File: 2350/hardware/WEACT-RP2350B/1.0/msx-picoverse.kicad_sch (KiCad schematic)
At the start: 10 parts, among them J1 Micro_SD_Card, U1 WEACT-RP2350B

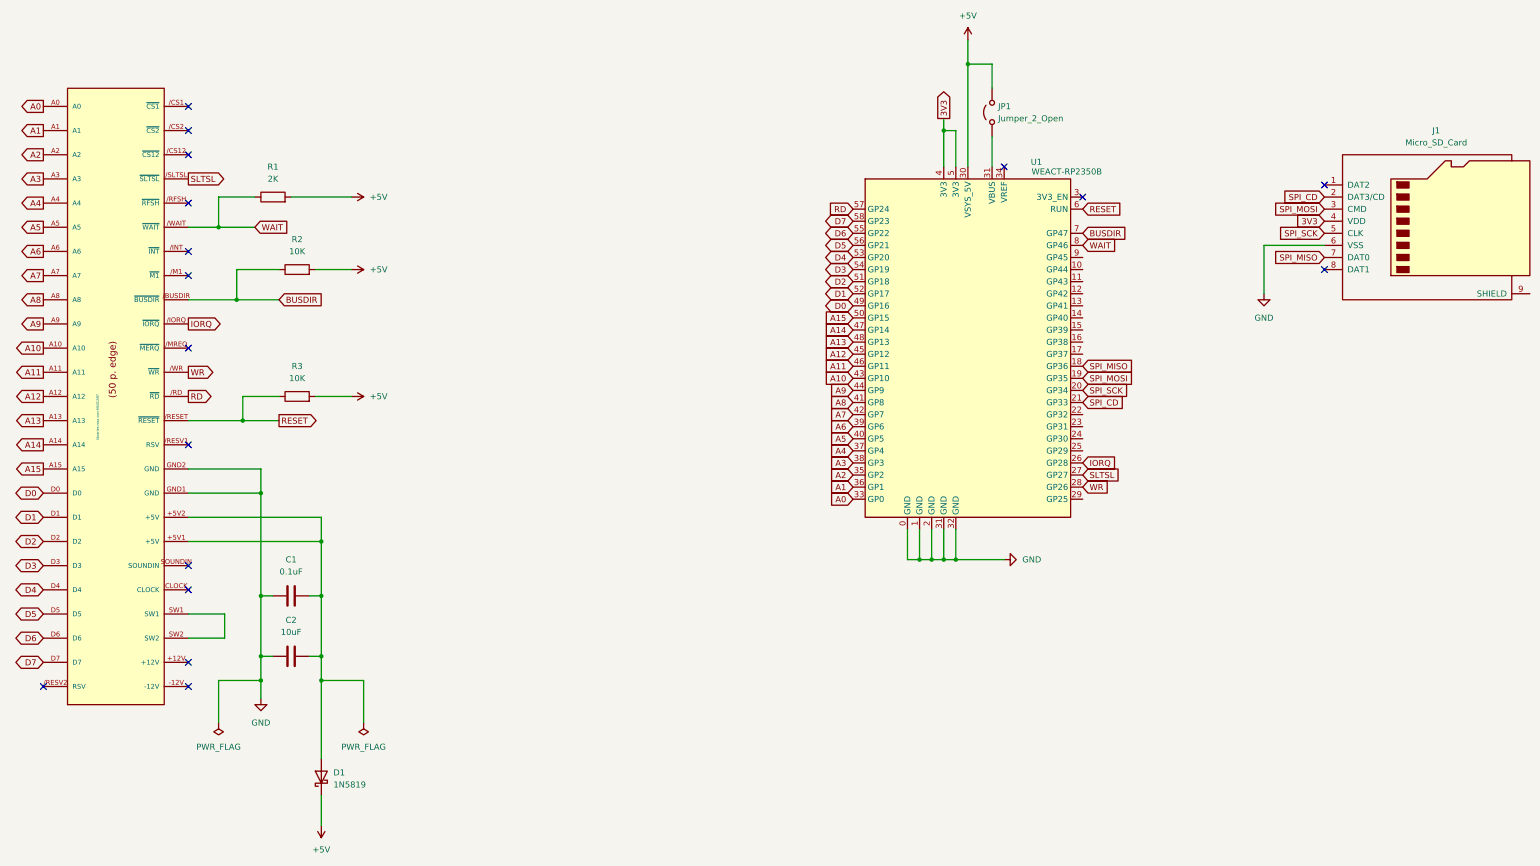
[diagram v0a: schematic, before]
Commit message: microSD card slot circuit update for 2350
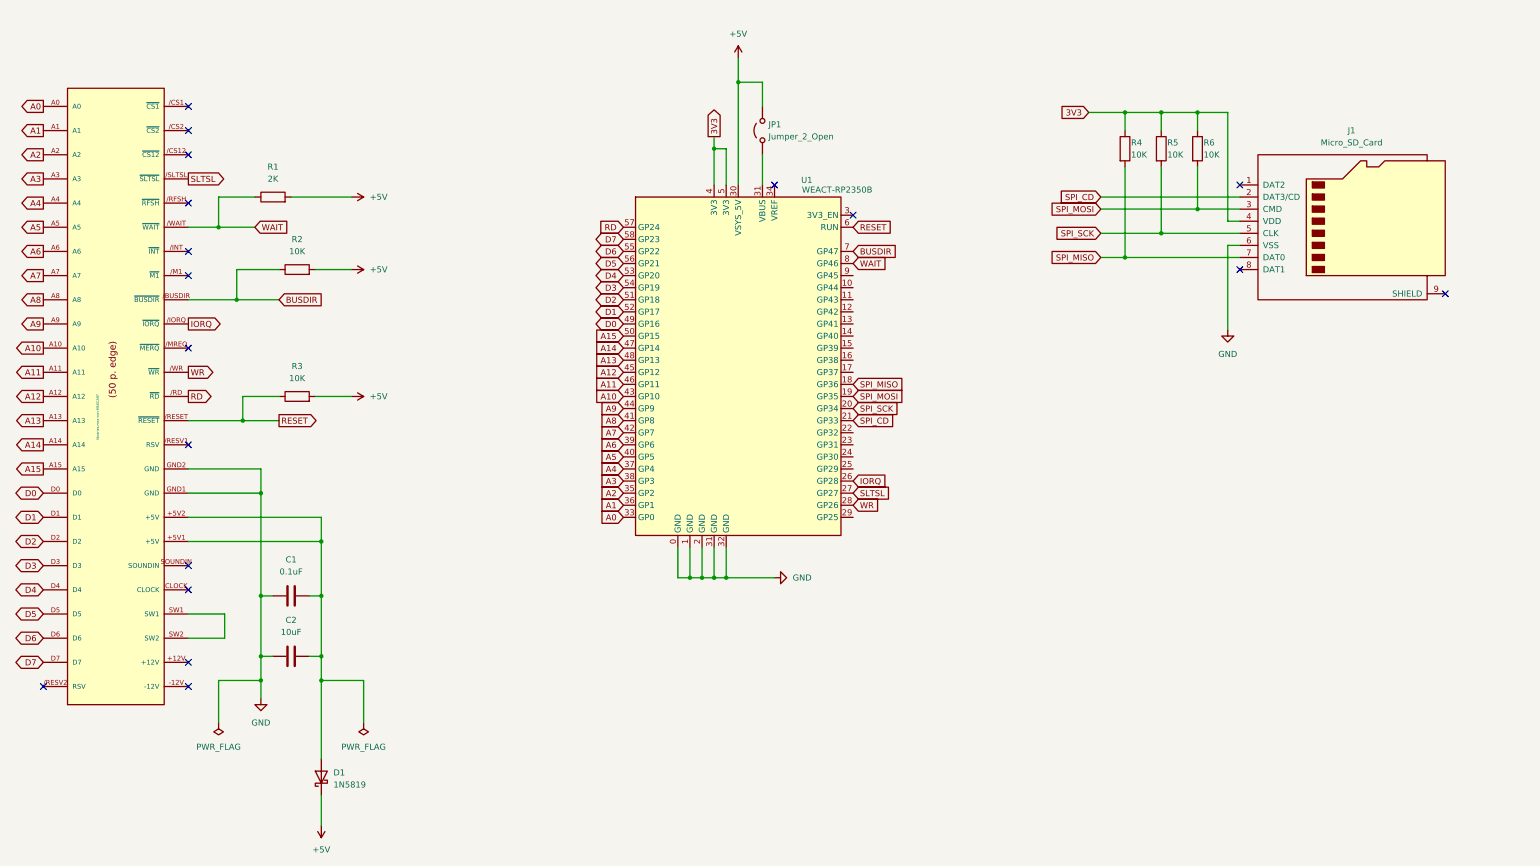
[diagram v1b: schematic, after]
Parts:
- added R4, R5, R6: 10K, symbol Device:R
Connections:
- net 3V3: now also R4.1, R5.1, R6.1
- net SPI_MISO: now also R4.2
- net SPI_MOSI: now also R6.2
- net SPI_SCK: now also R5.2
- no-connect marks 17 -> 18
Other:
- moved on the sheet: J1, JP1, U1
